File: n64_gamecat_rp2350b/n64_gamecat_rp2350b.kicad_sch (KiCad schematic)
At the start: 3 parts, among them U4 RP235x-B

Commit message: V0.6 PCB
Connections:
- net ALE_H: now also U4.37 (GPIO36); no longer U4.35 (GPIO34)
- net ALE_L: now also U4.38 (GPIO37); no longer U4.34 (GPIO33)
- net CO_AD0: now also U4.9 (GPIO8); no longer U4.42 (GPIO41)
- net CO_AD1: now also U4.7 (GPIO6); no longer U4.44 (GPIO43)
- net CO_AD10: now also U4.36 (GPIO35); no longer U4.51 (GPIO50)
- net CO_AD11: now also U4.2 (GPIO1); no longer U4.49 (GPIO48)
- net CO_AD12: now also U4.4 (GPIO3); no longer U4.47 (GPIO46)
- net CO_AD13: now also U4.6 (GPIO5); no longer U4.45 (GPIO44)
- net CO_AD14: now also U4.8 (GPIO7); no longer U4.43 (GPIO42)
- net CO_AD15: now also U4.10 (GPIO9); no longer U4.41 (GPIO40)
- net CO_AD2: now also U4.5 (GPIO4); no longer U4.46 (GPIO45)
- net CO_AD3: now also U4.3 (GPIO2); no longer U4.48 (GPIO47)
- net CO_AD4: now also U4.1 (GPIO0); no longer U4.50 (GPIO49)
- net CO_AD5: now also U4.35 (GPIO34); no longer U4.52 (GPIO51)
- net CO_AD6: now also U4.33 (GPIO32); no longer U4.54 (GPIO53)
- net CO_AD7: now also U4.31 (GPIO30); no longer U4.56 (GPIO55)
- net CO_AD8: now also U4.32 (GPIO31); no longer U4.55 (GPIO54)
- net CO_AD9: now also U4.34 (GPIO33); no longer U4.53 (GPIO52)
- net READ: now also U4.40 (GPIO39); no longer U4.32 (GPIO31)
- net WRITE: now also U4.39 (GPIO38); no longer U4.33 (GPIO32)

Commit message: v0.7 PCB; prep for 2350
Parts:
- added J1, J2: Conn_01x03_Pin, Connector_PinHeader_2.54mm:PinHeader_1x03_P2.54mm_Vertical, symbol Connector:Conn_01x03_Pin
- added J4: Conn_01x04_Pin, Connector_PinSocket_2.54mm:PinSocket_1x04_P2.54mm_Vertical, symbol Connector:Conn_01x04_Pin
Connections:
- net CO_AD0: now also U4.11 (GPIO10); no longer U4.9 (GPIO8)
- net CO_AD1: now also U4.9 (GPIO8); no longer U4.7 (GPIO6)
- net CO_AD11: now also U4.4 (GPIO3); no longer U4.2 (GPIO1)
- net CO_AD12: now also U4.6 (GPIO5); no longer U4.4 (GPIO3)
- net CO_AD13: now also U4.8 (GPIO7); no longer U4.6 (GPIO5)
- net CO_AD14: now also U4.10 (GPIO9); no longer U4.8 (GPIO7)
- net CO_AD15: now also U4.12 (GPIO11); no longer U4.10 (GPIO9)
- net CO_AD2: now also U4.7 (GPIO6); no longer U4.5 (GPIO4)
- net CO_AD3: now also U4.5 (GPIO4); no longer U4.3 (GPIO2)
- net CO_AD4: now also U4.3 (GPIO2); no longer U4.1 (GPIO0)
- net GND: now also U4.51 (GPIO50), J1.2 (Pin_2), J2.2 (Pin_2), J4.4 (Pin_4)
- net 5V: now reaches U4.53 (GPIO52)
- net 5V: now also J4.1 (Pin_1)
- net USB D-: now reaches U4.55 (GPIO54)
- net USB D-: now also J4.2 (Pin_2)
- net USB D+: now reaches U4.56 (GPIO55)
- net USB D+: now also J4.3 (Pin_3)
- net SWDIO: now reaches U4.57 (GPIO56)
- net SWDIO: now also J1.3 (Pin_3)
- net SWCLK: now reaches U4.58 (GPIO57)
- net SWCLK: now also J1.1 (Pin_1)
- new net RX0: J2.3 (Pin_3), U4.2 (GPIO1)
- new net TX0: J2.1 (Pin_1), U4.1 (GPIO0)

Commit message: Add v0.8 PCB
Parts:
- removed J4: Conn_01x04_Pin, Connector_PinSocket_2.54mm:PinSocket_1x04_P2.54mm_Vertical, symbol Connector:Conn_01x04_Pin
- added J3: Conn_01x05, Connector_PinSocket_2.54mm:PinSocket_1x05_P2.54mm_Vertical, symbol Connector_Generic:Conn_01x05
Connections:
- net 5V: now also J3.1 (Pin_1)
- net ALE_H: now also U4.35 (GPIO34); no longer U4.37 (GPIO36)
- net ALE_L: now also U4.36 (GPIO35); no longer U4.38 (GPIO37)
- net CA_AD0: now also U4.3 (GPIO2); no longer U4.29 (GPIO28)
- net CA_AD1: now also U4.4 (GPIO3); no longer U4.27 (GPIO26)
- net CA_AD10: now also U4.13 (GPIO12); no longer U4.20 (GPIO19)
- net CA_AD11: now also U4.14 (GPIO13); no longer U4.22 (GPIO21)
- net CA_AD12: now also U4.15 (GPIO14); no longer U4.24 (GPIO23)
- net CA_AD13: now also U4.16 (GPIO15); no longer U4.26 (GPIO25)
- net CA_AD14: now also U4.17 (GPIO16); no longer U4.28 (GPIO27)
- net CA_AD15: now also U4.18 (GPIO17); no longer U4.30 (GPIO29)
- net CA_AD2: now also U4.5 (GPIO4); no longer U4.25 (GPIO24)
- net CA_AD3: now also U4.6 (GPIO5); no longer U4.23 (GPIO22)
- net CA_AD4: now also U4.7 (GPIO6); no longer U4.21 (GPIO20)
- net CA_AD5: now also U4.8 (GPIO7); no longer U4.19 (GPIO18)
- net CA_AD6: now also U4.9 (GPIO8); no longer U4.17 (GPIO16)
- net CA_AD7: now also U4.10 (GPIO9); no longer U4.15 (GPIO14)
- net CA_AD8: now also U4.11 (GPIO10); no longer U4.16 (GPIO15)
- net CA_AD9: now also U4.12 (GPIO11); no longer U4.18 (GPIO17)
- net CO_AD0: now also U4.19 (GPIO18); no longer U4.11 (GPIO10)
- net CO_AD1: now also U4.20 (GPIO19); no longer U4.9 (GPIO8)
- net CO_AD10: now also U4.29 (GPIO28); no longer U4.36 (GPIO35)
- net CO_AD11: now also U4.30 (GPIO29); no longer U4.4 (GPIO3)
- net CO_AD12: now also U4.31 (GPIO30); no longer U4.6 (GPIO5)
- net CO_AD13: now also U4.32 (GPIO31); no longer U4.8 (GPIO7)
- net CO_AD14: now also U4.33 (GPIO32); no longer U4.10 (GPIO9)
- net CO_AD15: now also U4.34 (GPIO33); no longer U4.12 (GPIO11)
- net CO_AD2: now also U4.21 (GPIO20); no longer U4.7 (GPIO6)
- net CO_AD3: now also U4.22 (GPIO21); no longer U4.5 (GPIO4)
- net CO_AD4: now also U4.23 (GPIO22); no longer U4.3 (GPIO2)
- net CO_AD5: now also U4.24 (GPIO23); no longer U4.35 (GPIO34)
- net CO_AD6: now also U4.25 (GPIO24); no longer U4.33 (GPIO32)
- net CO_AD7: now also U4.26 (GPIO25); no longer U4.31 (GPIO30)
- net CO_AD8: now also U4.27 (GPIO26); no longer U4.32 (GPIO31)
- net CO_AD9: now also U4.28 (GPIO27); no longer U4.34 (GPIO33)
- net GND: now also J3.5 (Pin_5)
- net READ: now also U4.38 (GPIO37); no longer U4.40 (GPIO39)
- net USB D+: now also J3.3 (Pin_3)
- net USB D-: now also J3.2 (Pin_2)
- net WRITE: now also U4.37 (GPIO36); no longer U4.39 (GPIO38)

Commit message: Add v0.9 PCB
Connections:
- net ALE_H: now also U4.41 (GPIO40); no longer U4.35 (GPIO34)
- net ALE_L: now also U4.42 (GPIO41); no longer U4.36 (GPIO35)
- net CA_AD0: now also U4.1 (GPIO0); no longer U4.3 (GPIO2)
- net CA_AD1: now also U4.2 (GPIO1); no longer U4.4 (GPIO3)
- net CA_AD10: now also U4.11 (GPIO10); no longer U4.13 (GPIO12)
- net CA_AD11: now also U4.12 (GPIO11); no longer U4.14 (GPIO13)
- net CA_AD12: now also U4.13 (GPIO12); no longer U4.15 (GPIO14)
- net CA_AD13: now also U4.14 (GPIO13); no longer U4.16 (GPIO15)
- net CA_AD14: now also U4.15 (GPIO14); no longer U4.17 (GPIO16)
- net CA_AD15: now also U4.16 (GPIO15); no longer U4.18 (GPIO17)
- net CA_AD2: now also U4.3 (GPIO2); no longer U4.5 (GPIO4)
- net CA_AD3: now also U4.4 (GPIO3); no longer U4.6 (GPIO5)
- net CA_AD4: now also U4.5 (GPIO4); no longer U4.7 (GPIO6)
- net CA_AD5: now also U4.6 (GPIO5); no longer U4.8 (GPIO7)
- net CA_AD6: now also U4.7 (GPIO6); no longer U4.9 (GPIO8)
- net CA_AD7: now also U4.8 (GPIO7); no longer U4.10 (GPIO9)
- net CA_AD8: now also U4.9 (GPIO8); no longer U4.11 (GPIO10)
- net CA_AD9: now also U4.10 (GPIO9); no longer U4.12 (GPIO11)
- net READ: now also U4.44 (GPIO43); no longer U4.38 (GPIO37)
- net RX0: now also U4.46 (GPIO45); no longer U4.2 (GPIO1)
- net TX0: now also U4.45 (GPIO44); no longer U4.1 (GPIO0)
- net WRITE: now also U4.43 (GPIO42); no longer U4.37 (GPIO36)

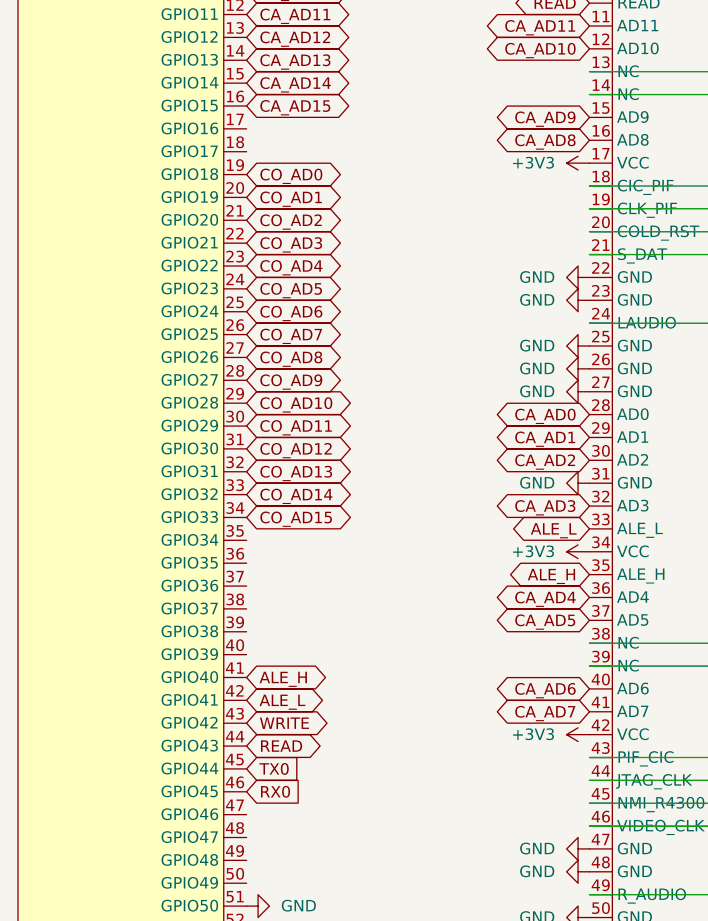
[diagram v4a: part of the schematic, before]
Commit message: Updates to improve DMA
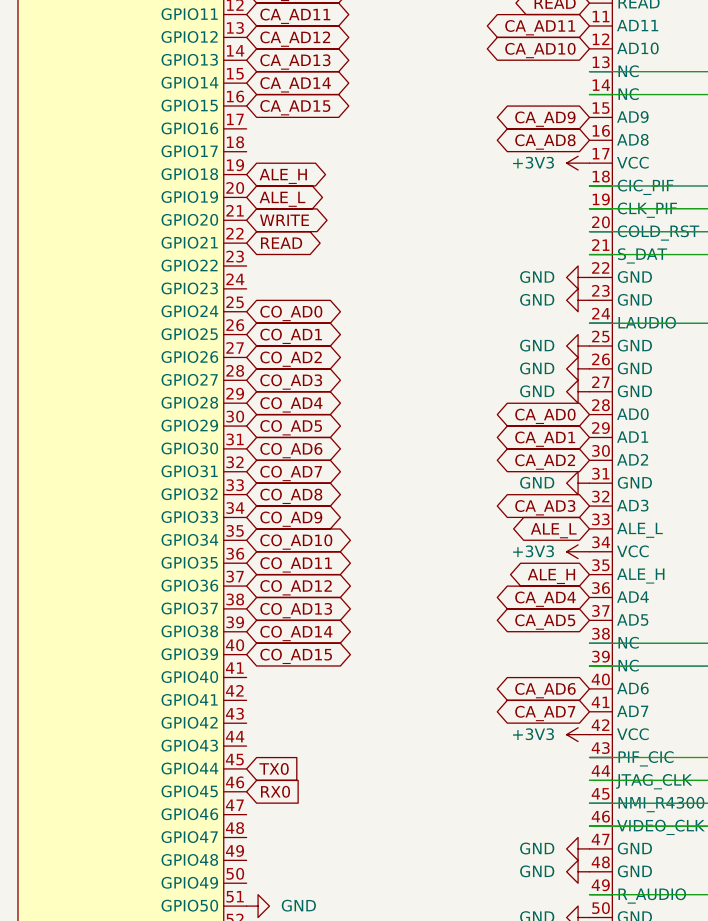
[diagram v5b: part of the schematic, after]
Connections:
- net ALE_H: now also U4.19 (GPIO18); no longer U4.41 (GPIO40)
- net ALE_L: now also U4.20 (GPIO19); no longer U4.42 (GPIO41)
- net CO_AD0: now also U4.25 (GPIO24); no longer U4.19 (GPIO18)
- net CO_AD1: now also U4.26 (GPIO25); no longer U4.20 (GPIO19)
- net CO_AD10: now also U4.35 (GPIO34); no longer U4.29 (GPIO28)
- net CO_AD11: now also U4.36 (GPIO35); no longer U4.30 (GPIO29)
- net CO_AD12: now also U4.37 (GPIO36); no longer U4.31 (GPIO30)
- net CO_AD13: now also U4.38 (GPIO37); no longer U4.32 (GPIO31)
- net CO_AD14: now also U4.39 (GPIO38); no longer U4.33 (GPIO32)
- net CO_AD15: now also U4.40 (GPIO39); no longer U4.34 (GPIO33)
- net CO_AD2: now also U4.27 (GPIO26); no longer U4.21 (GPIO20)
- net CO_AD3: now also U4.28 (GPIO27); no longer U4.22 (GPIO21)
- net CO_AD4: now also U4.29 (GPIO28); no longer U4.23 (GPIO22)
- net CO_AD5: now also U4.30 (GPIO29); no longer U4.24 (GPIO23)
- net CO_AD6: now also U4.31 (GPIO30); no longer U4.25 (GPIO24)
- net CO_AD7: now also U4.32 (GPIO31); no longer U4.26 (GPIO25)
- net CO_AD8: now also U4.33 (GPIO32); no longer U4.27 (GPIO26)
- net CO_AD9: now also U4.34 (GPIO33); no longer U4.28 (GPIO27)
- net READ: now also U4.22 (GPIO21); no longer U4.44 (GPIO43)
- net WRITE: now also U4.21 (GPIO20); no longer U4.43 (GPIO42)

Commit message: Misc changes; add OoT decomp
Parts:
- removed J1, J2: Conn_01x03_Pin, Connector_PinHeader_2.54mm:PinHeader_1x03_P2.54mm_Vertical, symbol Connector:Conn_01x03_Pin
- removed J3: Conn_01x05, Connector_PinSocket_2.54mm:PinSocket_1x05_P2.54mm_Vertical, symbol Connector_Generic:Conn_01x05
- removed U2: ~, n64_library:N64_cartridge_connecter_2.5mm, symbol n64:cartridge_connector
- removed U3: ~, n64_library:N64_cartridge_pins_2.5mm, symbol n64:console_connector
- removed U4: RP235x-B, RP2xxx_Stamp:RP2xxx_Stamp_XL_THT, symbol MCU_RaspberryPi2:RP2350B_Stamp_XL
- added A1: RaspberryPi_Pico, Module:RaspberryPi_Pico_Common_Unspecified, symbol MCU_Module:RaspberryPi_Pico
- added C1: 10uF, Capacitor_SMD:C_0805_2012Metric, symbol Device:C_US
- added C2, C3, C4, C5: 100nF, Capacitor_SMD:C_0402_1005Metric, symbol Device:C_US
- added D1: LED, LED_SMD:LED_0402_1005Metric, symbol Device:LED
- added J4: Conn_01x02_Pin, Connector_PinHeader_2.54mm:PinHeader_1x02_P2.54mm_Vertical, symbol Connector:Conn_01x02_Pin
- added R1, R2, R3, R4: 10K, Resistor_SMD:R_0402_1005Metric, symbol Device:R
- added R5: 1K, Resistor_SMD:R_0402_1005Metric, symbol Device:R
- added SW1: SW_SPDT, Connector_PinSocket_2.54mm:PinSocket_1x03_P2.54mm_Vertical, symbol Switch:SW_SPDT
- added U1: (no value), n64_library:N64_cartridge_connecter_2.5mm, symbol n64:cartridge_connector
- added U2: (no value), n64_library:N64_cartridge_pins_2.5mm, symbol n64:console_connector
- added U3, U4: SN74CBTLV3245ADW, footprints:DW20, symbol 2026-04-17_18-55-28:SN74CBTLV3245ADW
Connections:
- net ALE_H: now also A1.22 (GPIO17), R4.2, U1.35 (ALE_H), U2.35 (ALE_H)
- net ALE_L: now also A1.21 (GPIO16), R3.2, U1.33 (ALE_L), U2.33 (ALE_L)
- net CA_AD0: now also U1.28 (AD0), U3.18 (B1)
- net CA_AD1: now also U1.29 (AD1), U3.17 (B2)
- net CA_AD10: now also U1.12 (AD10), U4.16 (B3)
- net CA_AD11: now also U1.11 (AD11), U4.15 (B4)
- net CA_AD12: now also U1.7 (AD12), U4.14 (B5)
- net CA_AD13: now also U1.5 (AD13), U4.13 (B6)
- net CA_AD14: now also U1.4 (AD14), U4.12 (B7)
- net CA_AD15: now also U1.3 (AD15), U4.11 (B8)
- net CA_AD2: now also U1.30 (AD2), U3.16 (B3)
- net CA_AD3: now also U1.32 (AD3), U3.15 (B4)
- net CA_AD4: now also U1.36 (AD4), U3.14 (B5)
- net CA_AD5: now also U1.37 (AD5), U3.13 (B6)
- net CA_AD6: now also U1.40 (AD6), U3.12 (B7)
- net CA_AD7: now also U1.41 (AD7), U3.11 (B8)
- net CA_AD8: now also U1.16 (AD8), U4.18 (B1)
- net CA_AD9: now also U1.15 (AD9), U4.17 (B2)
- net GND: now also A1.13 (GND), A1.18 (GND), A1.23 (GND), A1.28 (GND), A1.3 (GND), A1.33 (AGND), A1.38 (GND), A1.8 (GND), C1.1, C2.1, C3.1, C4.1, C5.1, D1.1 (K), J4.2 (Pin_2), R1.1, R3.1, R4.1, U1.1 (GND), U1.2 (GND), U1.22 (GND), U1.23 (GND), U1.25 (GND), U1.26 (GND), U1.27 (GND), U1.31 (GND), U1.47 (GND), U1.48 (GND), U1.50 (GND), U1.6 (GND), U2.1 (GND), U2.2 (GND), U2.22 (GND), U2.23 (GND), U2.25 (GND), U2.26 (GND), U2.27 (GND), U2.31 (GND), U2.47 (GND), U2.48 (GND), U2.50 (GND), U2.6 (GND), U3.10 (GND), U4.10 (GND)
- net READ: now also A1.24 (GPIO18), U1.10 (READ), U2.10 (READ)
- net WRITE: now also A1.25 (GPIO19), U1.8 (WRITE), U2.8 (WRITE)
- new net: D1.2 (A), R5.1
- new net 3V3_CART: C1.2, SW1.1 (A), U1.17 (VCC), U1.34 (VCC), U1.42 (VCC), U1.9 (VCC), U2.17 (VCC), U2.34 (VCC), U2.42 (VCC), U2.9 (VCC)
- new net 3V3_OUT: A1.36 (3V3), C2.2, C3.2, C4.2, R2.1, U3.20 (VCC), U4.20 (VCC)
- new net AD0: A1.1 (GPIO0), U2.28 (AD0), U3.2 (A1)
- new net AD1: A1.2 (GPIO1), U2.29 (AD1), U3.3 (A2)
- new net AD10: A1.14 (GPIO10), U2.12 (AD10), U4.4 (A3)
- new net AD11: A1.15 (GPIO11), U2.11 (AD11), U4.5 (A4)
- new net AD12: A1.16 (GPIO12), U2.7 (AD12), U4.6 (A5)
- new net AD13: A1.17 (GPIO13), U2.5 (AD13), U4.7 (A6)
- new net AD14: A1.19 (GPIO14), U2.4 (AD14), U4.8 (A7)
- new net AD15: A1.20 (GPIO15), U2.3 (AD15), U4.9 (A8)
- new net AD2: A1.4 (GPIO2), U2.30 (AD2), U3.4 (A3)
- new net AD3: A1.5 (GPIO3), U2.32 (AD3), U3.5 (A4)
- new net AD4: A1.6 (GPIO4), U2.36 (AD4), U3.6 (A5)
- new net AD5: A1.7 (GPIO5), U2.37 (AD5), U3.7 (A6)
- new net AD6: A1.9 (GPIO6), U2.40 (AD6), U3.8 (A7)
- new net AD7: A1.10 (GPIO7), U2.41 (AD7), U3.9 (A8)
- new net AD8: A1.11 (GPIO8), U2.16 (AD8), U4.2 (A1)
- new net AD9: A1.12 (GPIO9), U2.15 (AD9), U4.3 (A2)
- new net CART_EN: A1.26 (GPIO20), R1.2, U3.19 (*OE), U4.19 (*OE)
- new net CIC_PIF: U1.18 (CIC_PIF), U2.18 (CIC_PIF)
- new net CLK_PIF: U1.19 (CLK_PIF), U2.19 (CLK_PIF)
- new net COLD_RST: U1.20 (COLD_RST), U2.20 (COLD_RST)
- new net JTAG_CLK: U1.44 (JTAG_CLK), U2.44 (JTAG_CLK)
- new net KILL: A1.27 (GPIO21), J4.1 (Pin_1), R2.2
- new net LAUDIO: U1.24 (LAUDIO), U2.24 (LAUDIO)
- new net NC: U1.13 (NC), U1.14 (NC), U1.38 (NC), U1.39 (NC), U2.13 (NC), U2.14 (NC), U2.38 (NC), U2.39 (NC), U3.1 (NC), U4.1 (NC)
- new net NMI_R4300: U1.45 (NMI_R4300), U2.45 (NMI_R4300)
- new net PIF_CIC: U1.43 (PIF_CIC), U2.43 (PIF_CIC)
- new net R_AUDIO: U1.49 (R_AUDIO), U2.49 (R_AUDIO)
- new net STATUS_LED: A1.29 (GPIO22), R5.2
- new net S_DAT: U1.21 (S_DAT), U2.21 (S_DAT)
- new net VIDEO_CLK: U1.46 (VIDEO_CLK), U2.46 (VIDEO_CLK)
- new net VSYS: A1.39 (VSYS), C5.2, SW1.2 (B)
- no-connect marks 0 -> 1
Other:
- note added: "CARTRIDGE"
- note added: "CONSOLE"
